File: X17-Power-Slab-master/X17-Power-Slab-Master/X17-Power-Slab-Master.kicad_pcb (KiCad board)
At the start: 2 copper layers, 129.5 x 99 mm, 31 parts, among them J1 Conn_01x12_Pin, J2 ET60T-D04-3-08-D04-X-R1-S, J3 796636-6, Q2 TSM340N06CP ROG

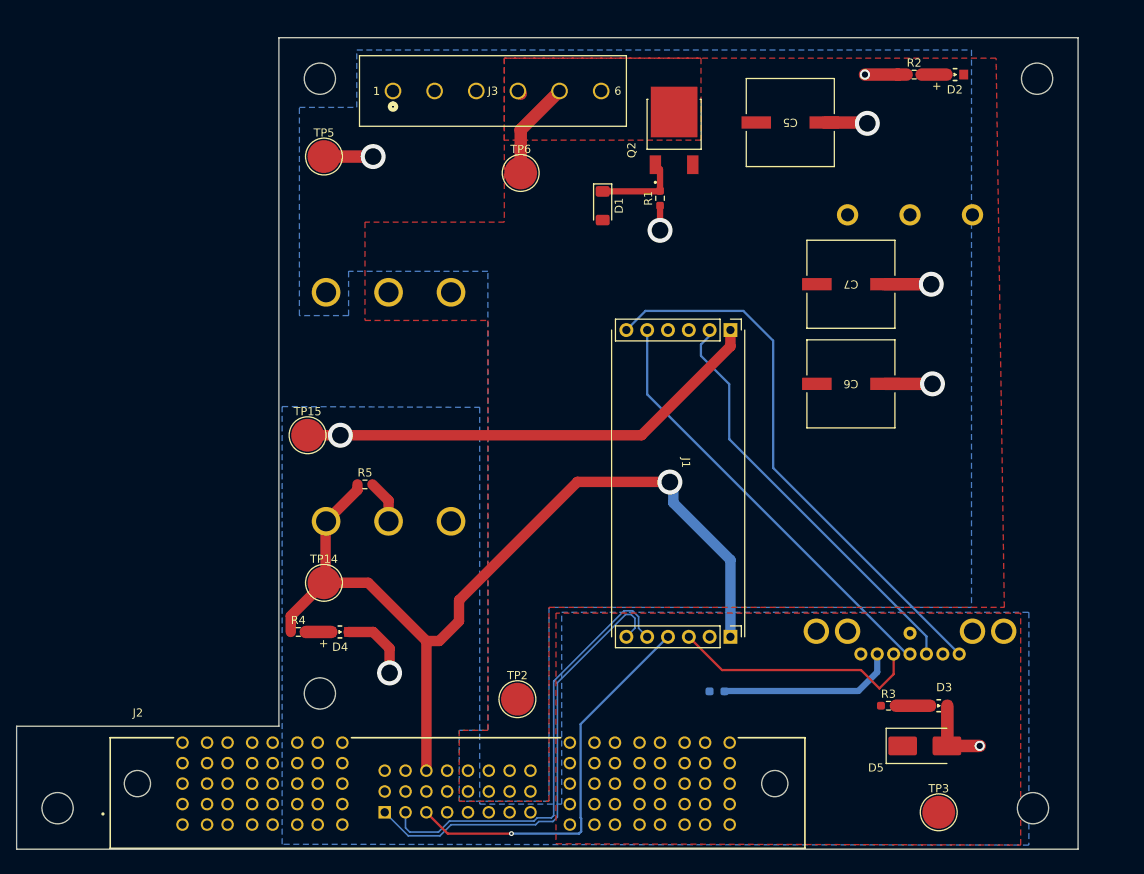
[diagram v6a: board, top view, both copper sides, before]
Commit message: silkscreen + pinout fixes
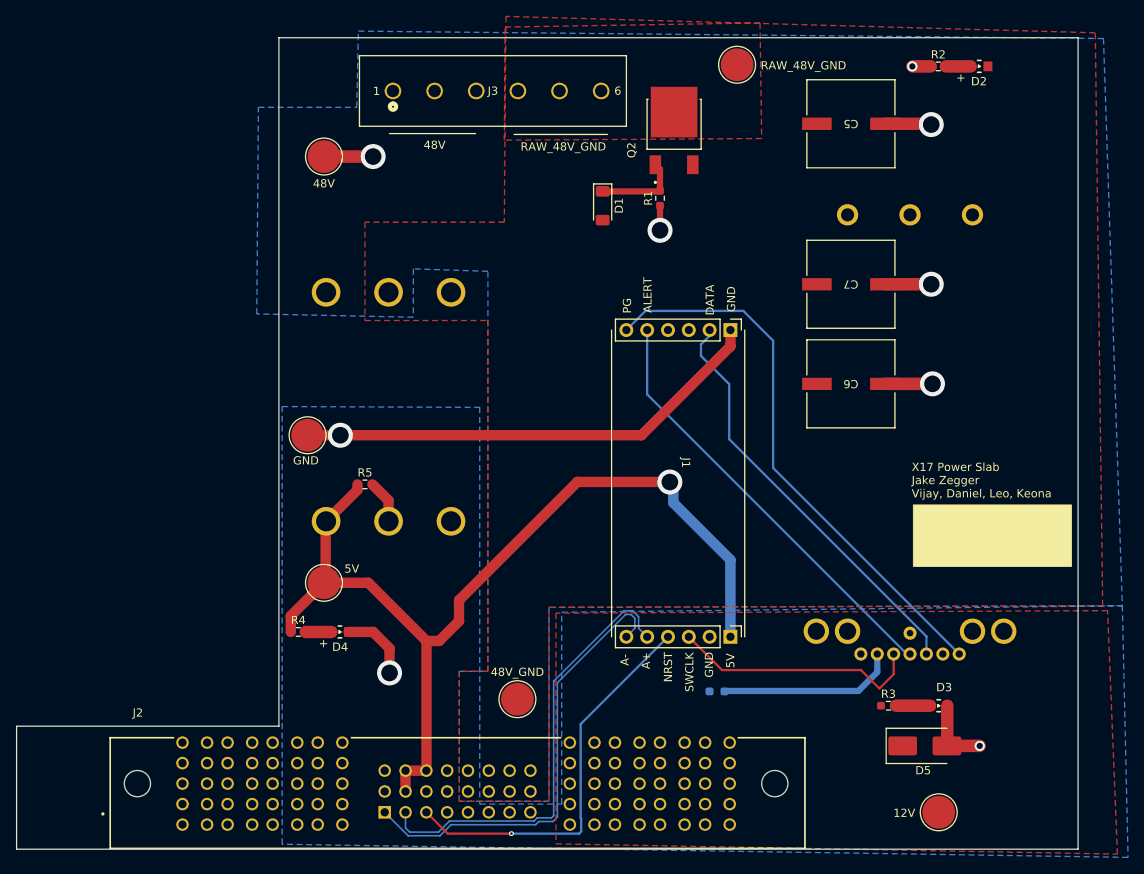
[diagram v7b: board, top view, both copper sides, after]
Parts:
- removed H1 (x3), H3, H4: 6-32-HOLE, X16_PowerSlab_V2:6-32-HOLE
- J2: footprint ET60T-D04-3-08-D04-X-R1-S:SAMTEC_ET60T-D04-3-08-D04-X-R1-S -> ET60T-D04-3-08-D04-S-R1-S:SAMTEC_ET60T-D04-3-08-D04-S-R1-S
- moved TP6 29.5 mm to (127.4, 46.8)
- moved C5 7.40 mm to (141.3, 54.0)
- moved D2 3.11 mm to (156.9, 47.0)
- moved R2 3.11 mm to (151.9, 47.0)
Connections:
- J2 pad 06: (no net) -> unconnected-(J2-Pad06)
- J2 pad 08: 48V_GND -> unconnected-(J2-Pad08)
- J2 pad 10: unconnected-(J2-Pad10) -> 5V
- J2 pad 11: unconnected-(J2-Pad11) -> 12V_5V_GND
- J2 pad 15: unconnected-(J2-Pad15) -> 48V_GND
- J2 pad 18: unconnected-(J2-Pad18) -> 5V
- J2 pad 23: (no net) -> 48V_GND
- J2 pad P08_1: 12V_5V_GND -> unconnected-(J2-P08-PadP08_1)
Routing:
- net RAW_48V_GND: track 12.7 -> 0.25 mm
- net 5V: track 114.7 -> 119.8 mm
- net 48V: track 30.7 -> 28.4 mm
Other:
- board text added: "12V"
- board text added: "48V"
- board text added: "48V_GND"
- board text added: "5V"
- board text added: "A+"
- board text added: "A-"
- board text added: "ALERT"
- board text added: "DATA"
- board text added: "GND"
- board text added: "NRST"
- board text added: "PG"
- board text added: "RAW_48V_GND"
- board text added: "SWCLK"
- board text added: "X17 Power Slab Jake Zegger Vijay, Daniel, Leo, Keona"

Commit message: some pinout changes
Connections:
- J2 pad 09: unconnected-(J2-Pad09) -> 12V_5V_GND
- J2 pad 10: 5V -> 12V_5V_GND
- J2 pad 11: 12V_5V_GND -> 5V
- J2 pad 12: 12V_5V_GND -> 5V
- J2 pad 17: unconnected-(J2-Pad17) -> 12V_5V_GND
- J2 pad 18: 5V -> 12V_5V_GND
- J2 pad 20: 12V_5V_GND -> 5V
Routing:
- net 5V: track 119.8 -> 122.3 mm
